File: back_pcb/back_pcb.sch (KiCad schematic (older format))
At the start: 111 parts, among them J1 Conn_01x12, P2 EXPANSION_BOTTOM, P3 EXPANSION_TOP, P4 AUDIO_CONN, P6 ATMEGA_HEADER, P7 EXPANSION_BOTTOM2, P8 JST, P9 USB_A, Q1 IRLML6401, Q2 IRLML6401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

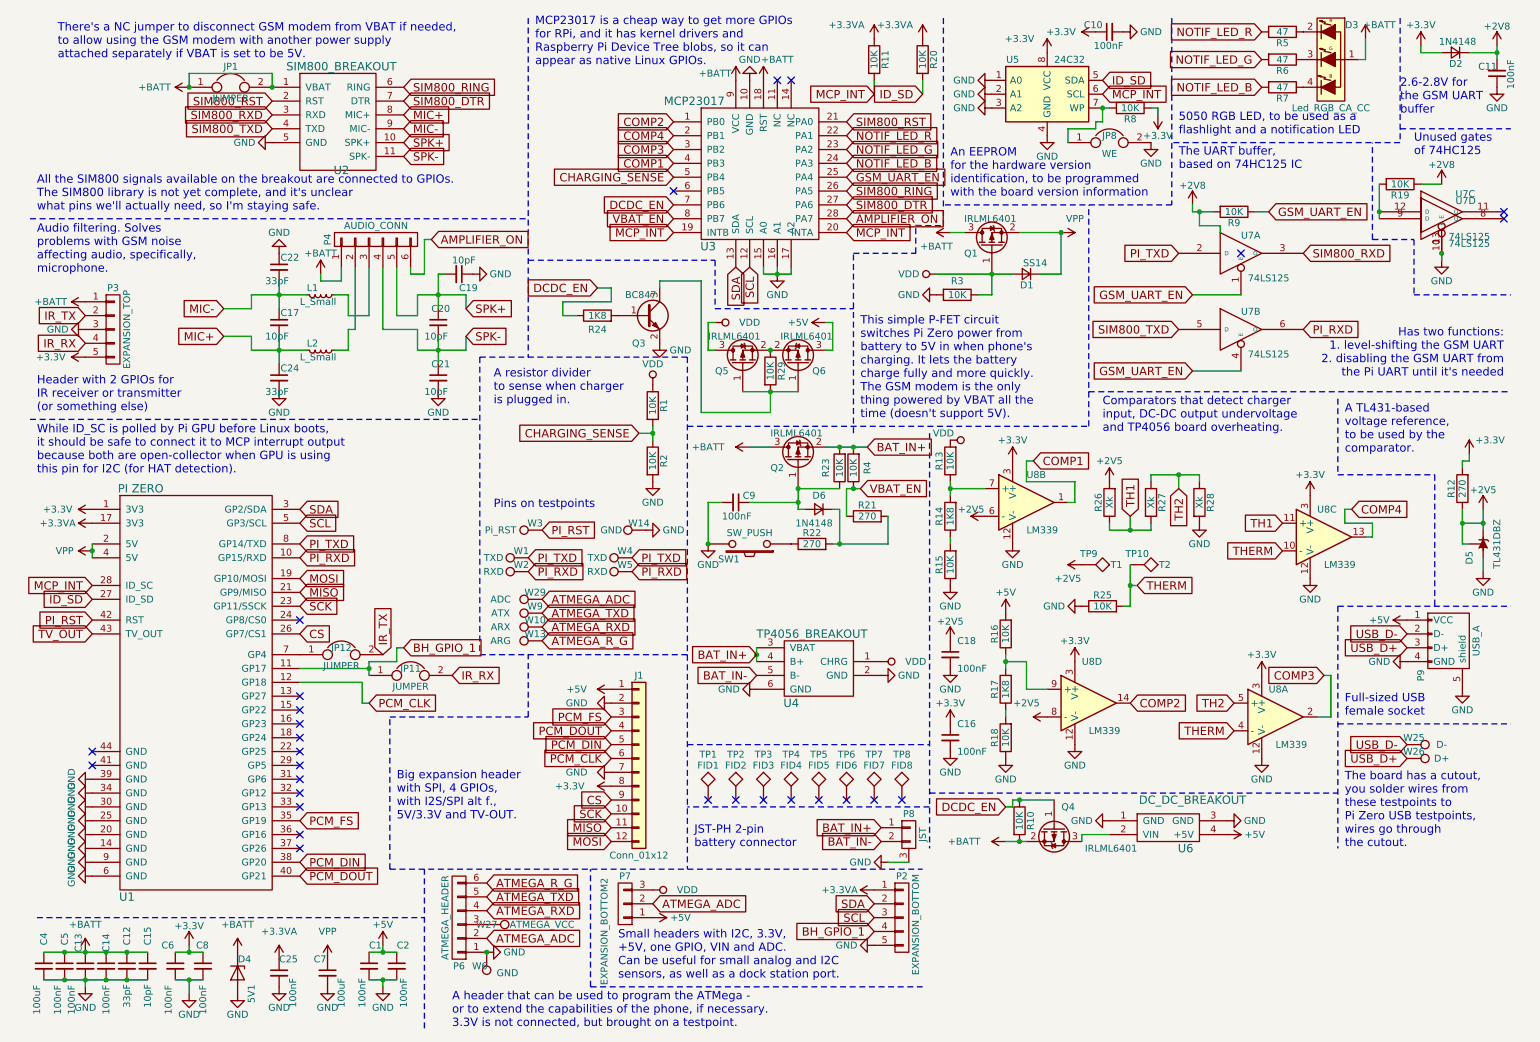
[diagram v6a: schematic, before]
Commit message: Changes towards Delta-B #69 #68 #67 #66 #64 #65 #63
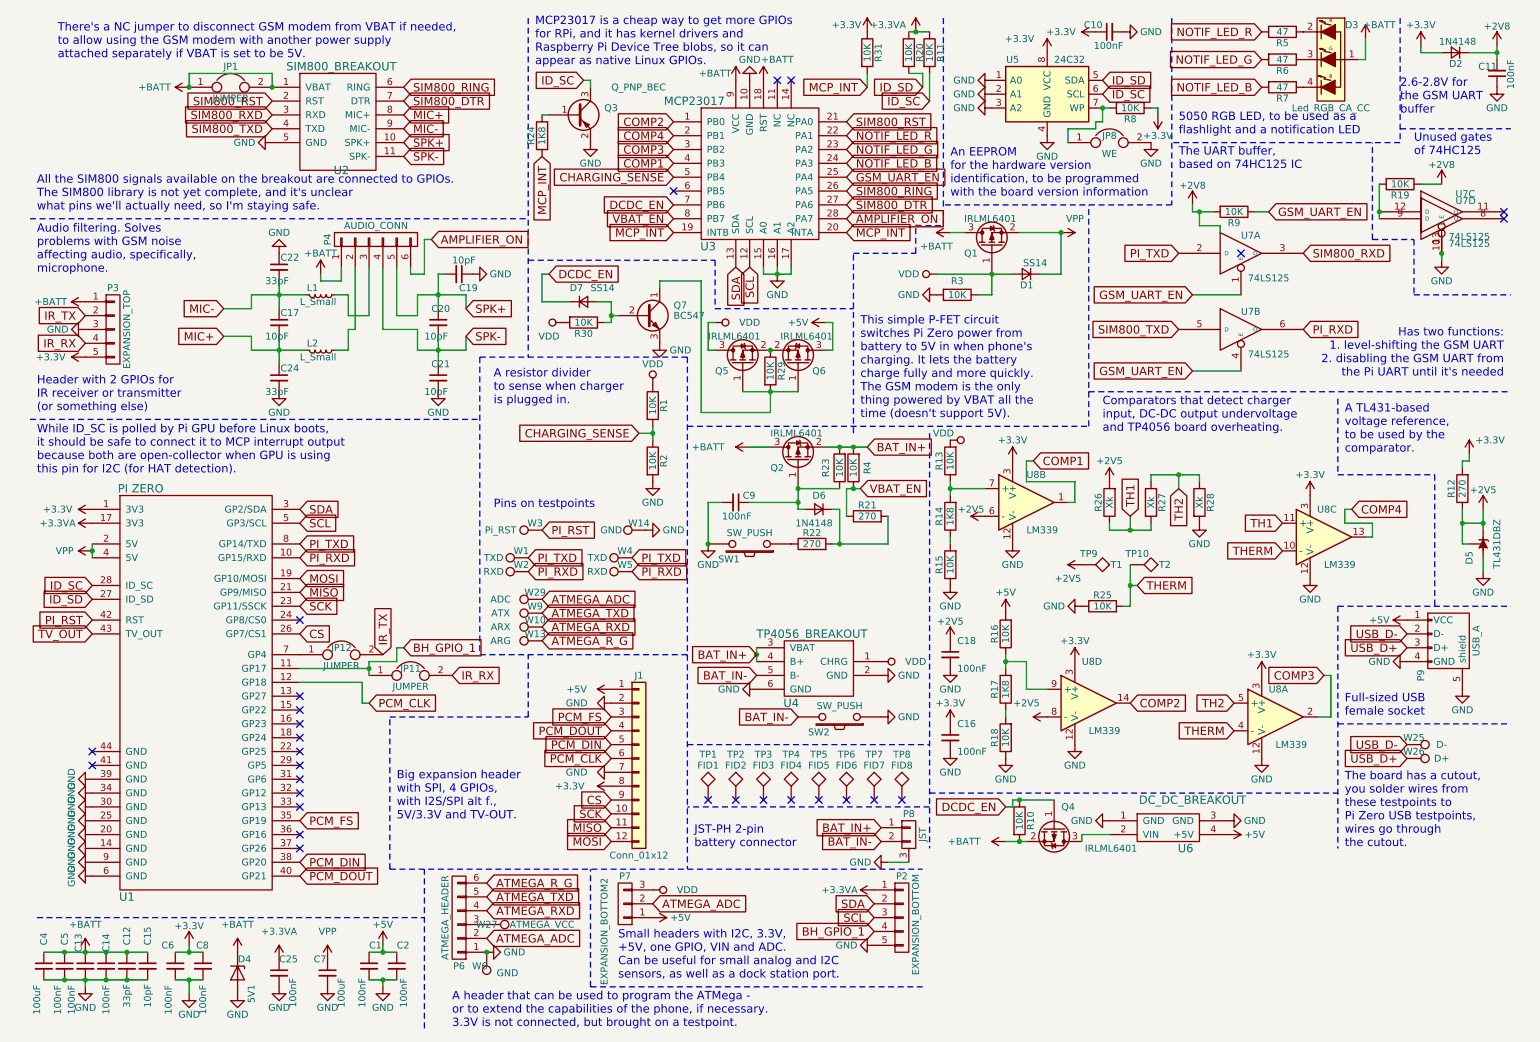
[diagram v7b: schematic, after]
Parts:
- removed Q3: BC847, common-footprints:BC847B-SOT-23_Handsoldering, symbol BC847
- added D7: SS14, Diodes_SMD:D_MiniMELF_Handsoldering, symbol D_Small
- added Q3: Q_PNP_BEC, TO_SOT_Packages_SMD:SOT-23_Handsoldering, symbol Q_PNP_BEC
- added Q7: BC547, common-footprints:BC847B-SOT-23_Handsoldering, symbol BC547
- added R30, R31: 10K, common-footprints:R_0805_10K_HandSoldering, symbol R
- added SW2: SW_PUSH, common-footprints:SW_SPST_EVQPE1, symbol SW_PUSH
- R12: footprint Resistors_SMD:R_0603_HandSoldering -> Resistors_SMD:R_0805_HandSoldering
- SW1: footprint footprints:SW_SPST_EVQPE1 -> common-footprints:SW_SPST_EVQPE1
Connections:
- net +3V3: now also R31.1
- net BAT_IN-: now also SW2.2
- net DCDC_EN: now also D7.1 (K); no longer R24.1
- net GND: now also Q3.2 (E), Q7.3 (E), SW2.1
- net MCP_INT: now also R24.1, R31.2; no longer R11.2, U1.28 (ID_SC), U5.6 (SCL)
- net VDD: now also R30.2
- net at Q5.1 (G), Q6.1 (G), R29.2: now also Q7.1 (C)
- net at R24.2: now also Q3.1 (B)
- new net: D7.2 (A), Q7.2 (B), R30.1
- new net ID_SC: Q3.3 (C), R11.2, U1.28 (ID_SC), U5.6 (SCL)
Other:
- moved on the sheet: R11, R20

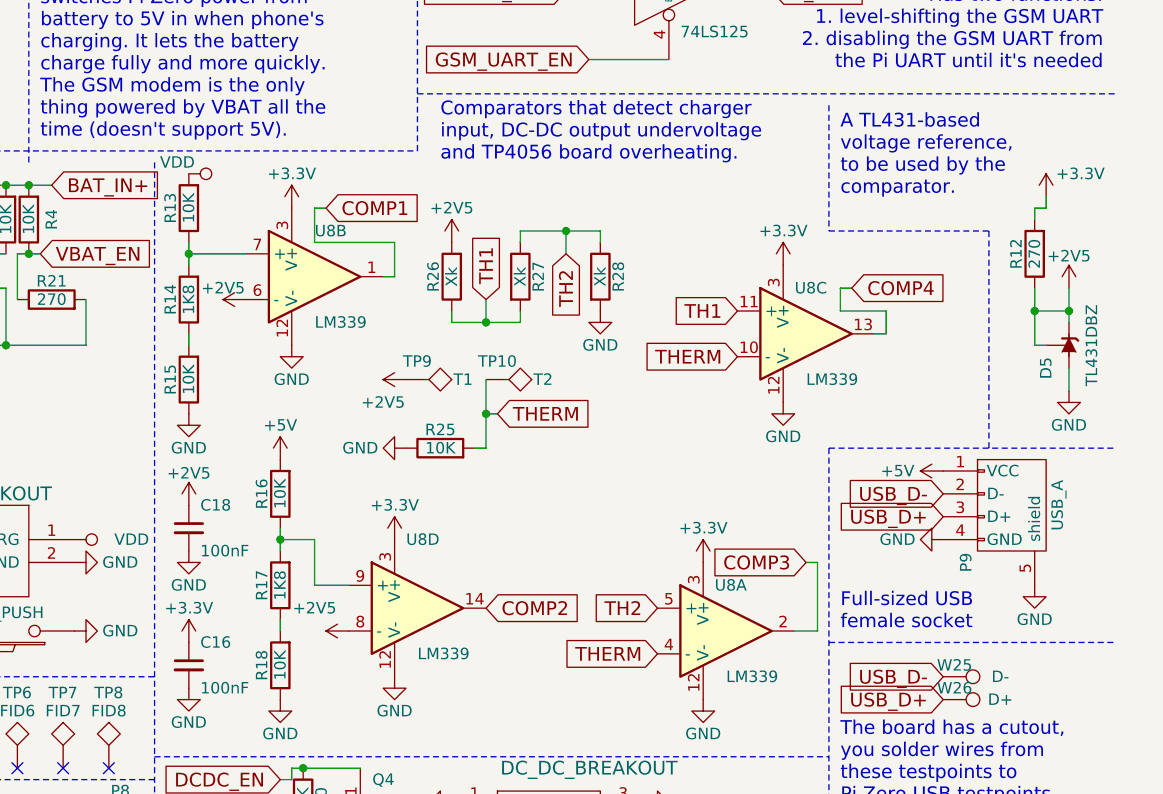
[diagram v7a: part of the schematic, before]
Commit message: Comparator reference now 1V2, changing text a little bit
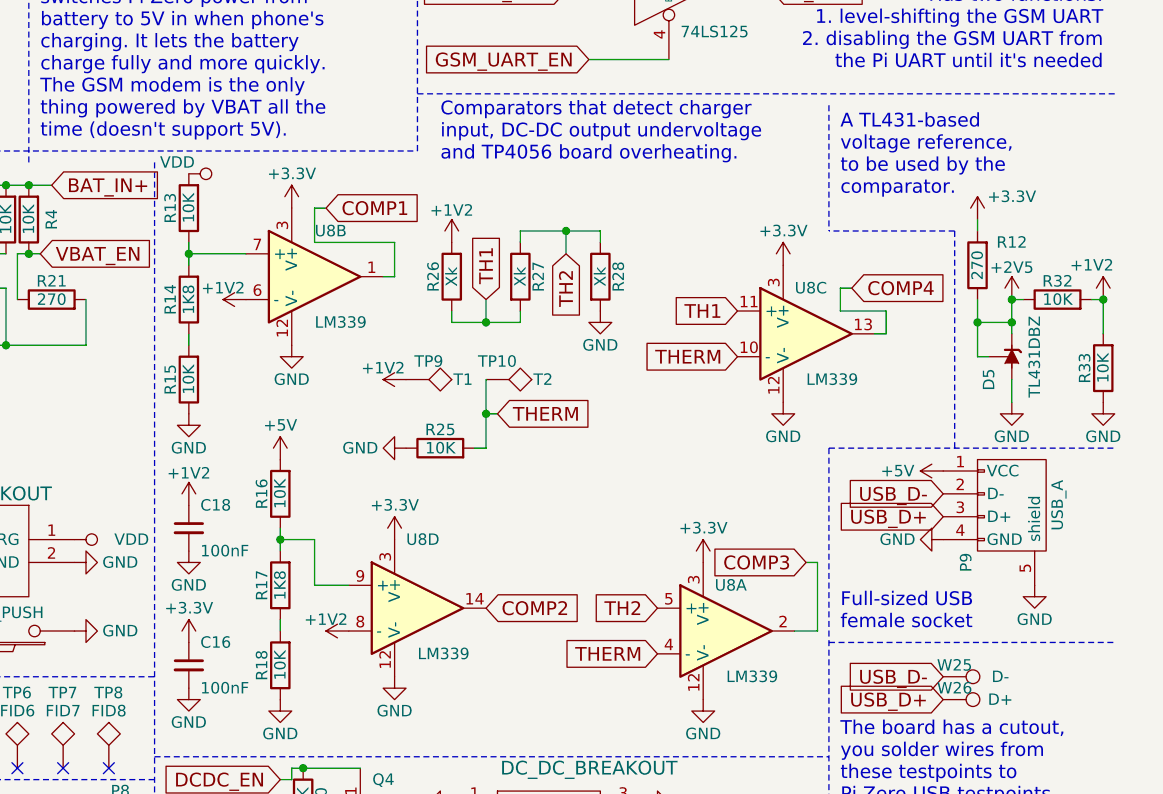
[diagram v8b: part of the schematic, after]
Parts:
- added R32, R33: 10K, common-footprints:R_0805_10K_HandSoldering, symbol R
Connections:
- net +2V5: now also R32.1; no longer C18.1, R26.2, TP9.1, U8.6 (-), U8.8 (-)
- net GND: now also R33.1
- new net +1V2: C18.1, R26.2, R32.2, R33.2, TP9.1, U8.6 (-), U8.8 (-)
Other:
- moved on the sheet: D5, R12
